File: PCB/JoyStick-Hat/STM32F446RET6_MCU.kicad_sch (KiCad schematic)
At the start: 42 parts, among them J1 20021121-00010C4LF, J16 Conn_01x06, J2 BU2032SM-JJ-GTR, J3 Conn_02x05_Odd_Even, SW1 TL3301NF260QG, U1 STM32F446VETx, X1 ABM3B-8.000MHZ-B2-T, X2 ABS07-32.768KHZ-9-T

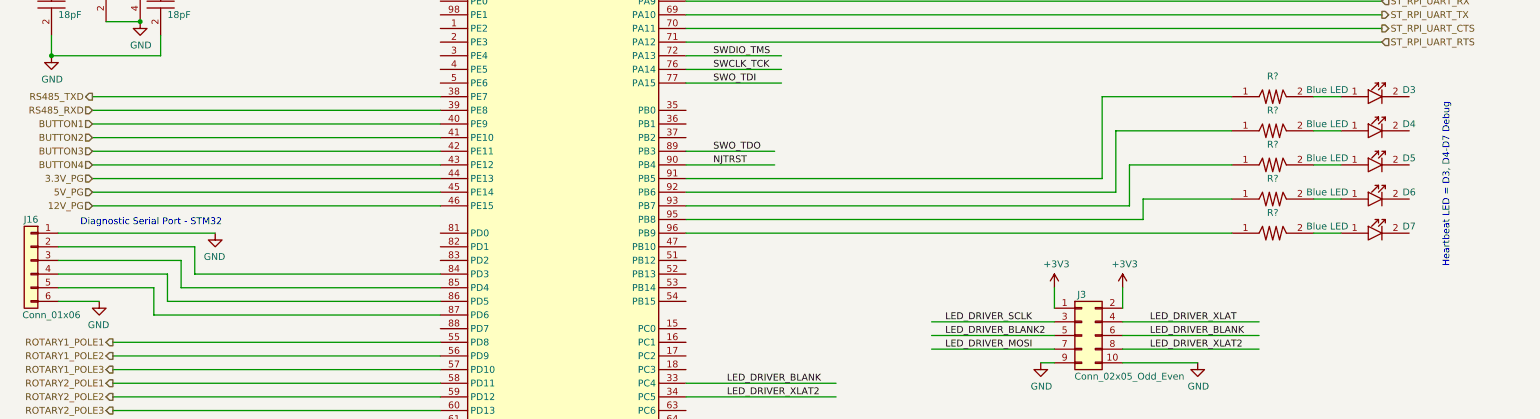
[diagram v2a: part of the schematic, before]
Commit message: Board Routing
Connectors swapped around and board route started
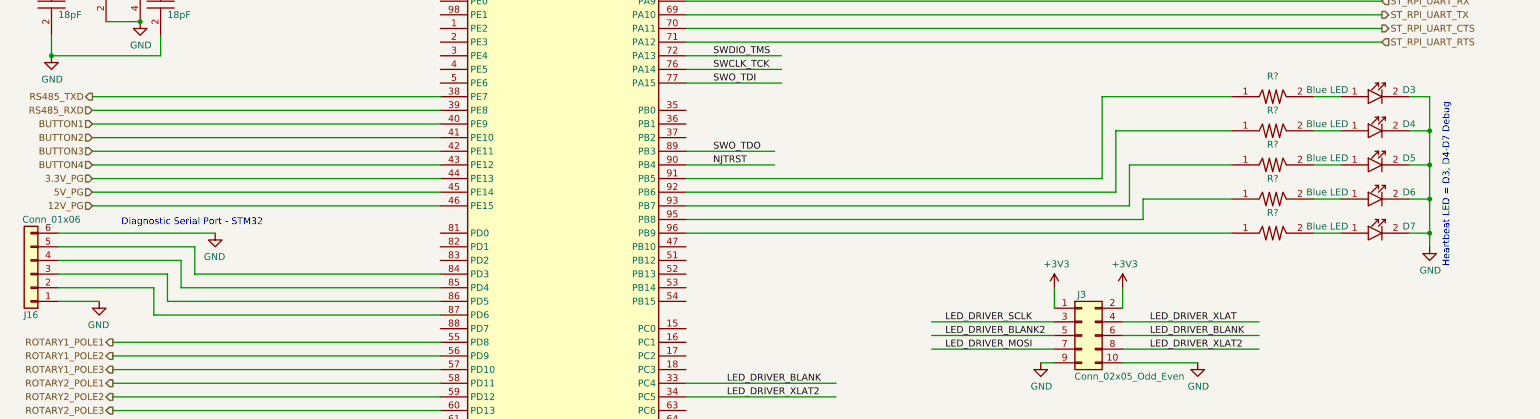
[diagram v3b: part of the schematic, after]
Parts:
- J16: footprint Connector_PinHeader_2.54mm:PinHeader_1x06_P2.54mm_Vertical -> Connector_PinHeader_2.54mm:PinHeader_1x06_P2.54mm_Horizontal
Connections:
- net GND: now also D3.2, D4.2, D5.2, D6.2, D7.2
- net at J16.2 (Pin_2): now also U1.87 (PD6); no longer U1.84 (PD3)
- net at J16.3 (Pin_3): now also U1.86 (PD5); no longer U1.85 (PD4)
- net at J16.4 (Pin_4): now also U1.85 (PD4); no longer U1.86 (PD5)
- net at J16.5 (Pin_5): now also U1.84 (PD3); no longer U1.87 (PD6)
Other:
- moved on the sheet: J16
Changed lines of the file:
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@@
   (junction (at 38.1 39.37) (diameter 0) (color 0 0 0 0)
   )
+  (junction (at 275.59 92.71) (diameter 0) (color 0 0 0 0)
+  )
   (junction (at 19.05 78.74) (diameter 0) (color 0 0 0 0)
   )
@@
   (junction (at 93.98 25.4) (diameter 0) (color 0 0 0 0)
   )
+  (junction (at 275.59 105.41) (diameter 0) (color 0 0 0 0)
+  )
   (junction (at 17.78 166.37) (diameter 0) (color 0 0 0 0)
   )
@@
   (junction (at 63.5 181.61) (diameter 0) (color 0 0 0 0)
   )
+  (junction (at 275.59 111.76) (diameter 0) (color 0 0 0 0)
+  )
   (junction (at 114.3 38.1) (diameter 0) (color 0 0 0 0)
   )
@@
   (junction (at 116.84 38.1) (diameter 0) (color 0 0 0 0)
   )
+  (junction (at 275.59 99.06) (diameter 0) (color 0 0 0 0)
+  )
   (junction (at 135.89 25.4) (diameter 0) (color 0 0 0 0)
   )
@@
     (stroke (width 0) (type default))
   )
-  (wire (pts (xy 20.32 119.38) (xy 40.64 119.38))
-    (stroke (width 0) (type default))
-  )
   (wire (pts (xy 26.67 88.9) (xy 91.44 88.9))
     (stroke (width 0) (type default))
@@
     (stroke (width 0) (type default))
   )
+  (wire (pts (xy 20.32 119.38) (xy 40.64 119.38))
+    (stroke (width 0) (type default))
+  )
   (wire (pts (xy 222.25 109.22) (xy 222.25 105.41))
     (stroke (width 0) (type default))
@@
     (stroke (width 0) (type default))
   )
+  (wire (pts (xy 275.59 105.41) (xy 275.59 111.76))
+    (stroke (width 0) (type default))
+  )
+  (wire (pts (xy 275.59 86.36) (xy 275.59 92.71))
+    (stroke (width 0) (type default))
+  )
+  (wire (pts (xy 20.32 116.84) (xy 43.18 116.84))
+    (stroke (width 0) (type default))
+  )
   (wire (pts (xy 19.05 33.02) (xy 19.05 39.37))
     (stroke (width 0) (type default))
@@
     (stroke (width 0) (type default))
   )
+  (wire (pts (xy 271.78 105.41) (xy 275.59 105.41))
+    (stroke (width 0) (type default))
+  )
   (wire (pts (xy 182.88 29.21) (xy 190.5 29.21))
     (stroke (width 0) (type default))
@@
     (stroke (width 0) (type default))
   )
+  (wire (pts (xy 271.78 92.71) (xy 275.59 92.71))
+    (stroke (width 0) (type default))
+  )
   (wire (pts (xy 175.26 29.21) (xy 182.88 29.21))
     (stroke (width 0) (type default))
@@
     (stroke (width 0) (type default))
   )
-  (wire (pts (xy 20.32 114.3) (xy 45.72 114.3))
-    (stroke (width 0) (type default))
-  )
   (wire (pts (xy 121.92 17.78) (xy 121.92 38.1))
     (stroke (width 0) (type default))
@@
     (stroke (width 0) (type default))
   )
+  (wire (pts (xy 275.59 111.76) (xy 275.59 114.3))
+    (stroke (width 0) (type default))
+  )
   (wire (pts (xy 116.84 177.8) (xy 114.3 177.8))
     (stroke (width 0) (type default))
@@
     (stroke (width 0) (type default))
   )
+  (wire (pts (xy 271.78 86.36) (xy 275.59 86.36))
+    (stroke (width 0) (type default))
+  )
   (wire (pts (xy 218.44 130.81) (xy 243.84 130.81))
     (stroke (width 0) (type default))
@@
     (stroke (width 0) (type default))
   )
+  (wire (pts (xy 20.32 114.3) (xy 45.72 114.3))
+    (stroke (width 0) (type default))
+  )
   (wire (pts (xy 254 111.76) (xy 259.08 111.76))
     (stroke (width 0) (type default))
@@
     (stroke (width 0) (type default))
   )
+  (wire (pts (xy 20.32 121.92) (xy 38.1 121.92))
+    (stroke (width 0) (type default))
+  )
   (wire (pts (xy 30.48 170.18) (xy 63.5 170.18))
     (stroke (width 0) (type default))
@@
     (stroke (width 0) (type default))
   )
+  (wire (pts (xy 275.59 92.71) (xy 275.59 99.06))
+    (stroke (width 0) (type default))
+  )
   (wire (pts (xy 114.3 177.8) (xy 114.3 181.61))
     (stroke (width 0) (type default))
@@
     (stroke (width 0) (type default))
   )
+  (wire (pts (xy 275.59 99.06) (xy 275.59 105.41))
+    (stroke (width 0) (type default))
+  )
   (wire (pts (xy 137.16 152.4) (xy 204.47 152.4))
     (stroke (width 0) (type default))
   )
-  (wire (pts (xy 88.9 180.34) (xy 88.9 191.77))
+  (wire (pts (xy 271.78 111.76) (xy 275.59 111.76))
     (stroke (width 0) (type default))
   )
-  (wire (pts (xy 38.1 121.92) (xy 20.32 121.92))
+  (wire (pts (xy 88.9 180.34) (xy 88.9 191.77))
     (stroke (width 0) (type default))
   )
-  (wire (pts (xy 20.32 111.76) (xy 49.53 111.76))
+  (wire (pts (xy 271.78 99.06) (xy 275.59 99.06))
     (stroke (width 0) (type default))
   )
@@
     (stroke (width 0) (type default))
   )
-  (wire (pts (xy 43.18 116.84) (xy 20.32 116.84))
+  (wire (pts (xy 111.76 38.1) (xy 114.3 38.1))
     (stroke (width 0) (type default))
   )
-  (wire (pts (xy 111.76 38.1) (xy 114.3 38.1))
+  (wire (pts (xy 20.32 111.76) (xy 49.53 111.76))
     (stroke (width 0) (type default))
   )
@@
     (effects (font (size 4 4) (thickness 0.8) bold) (justify left bottom))
   )
-  (text "Diagnostic Serial Port - STM32" (at 50.8 110.49 0)
+  (text "Diagnostic Serial Port - STM32" (at 58.42 110.49 0)
     (effects (font (size 1.27 1.27)) (justify right bottom))
   )
@@
     )
   )
-  (symbol (lib_id "Connector_Generic:Conn_01x06") (at 15.24 116.84 0) (mirror y) (unit 1)
+  (symbol (lib_id "Connector_Generic:Conn_01x06") (at 15.24 119.38 180) (unit 1)
     (in_bom yes) (on_board yes) (dnp no)
-    (property "Reference" "J16" (at 15.24 109.22 0)
+    (property "Reference" "J16" (at 15.24 127 0)
       (effects (font (size 1.27 1.27)))
     )
-    (property "Value" "Conn_01x06" (at 19.05 127 0)
+    (property "Value" "Conn_01x06" (at 19.05 109.22 0)
       (effects (font (size 1.27 1.27)))
     )
-    (property "Footprint" "Connector_PinHeader_2.54mm:PinHeader_1x06_P2.54mm_Vertical" (at 15.24 116.84 0)
+    (property "Footprint" "Connector_PinHeader_2.54mm:PinHeader_1x06_P2.54mm_Horizontal" (at 15.24 119.38 0)
       (effects (font (size 1.27 1.27)) hide)
     )
-    (property "Datasheet" "~" (at 15.24 116.84 0)
+    (property "Datasheet" "~" (at 15.24 119.38 0)
       (effects (font (size 1.27 1.27)) hide)
     )
@@
         )
       )
+    )
+  )
+  (symbol (lib_id "power:GND") (at 275.59 114.3 0) (unit 1)
+    (in_bom yes) (on_board yes) (dnp no)
+    (property "Reference" "#PWR022" (at 275.59 120.65 0)
+      (effects (font (size 1.27 1.27)) hide)
+    )
+    (property "Value" "GND" (at 275.717 118.6942 0)
+      (effects (font (size 1.27 1.27)))
+    )
+    (property "Footprint" "" (at 275.59 114.3 0)
+      (effects (font (size 1.27 1.27)) hide)
+    )
+    (property "Datasheet" "" (at 275.59 114.3 0)
+      (effects (font (size 1.27 1.27)) hide)
+    )
+    (pin "1")
+    (instances
+      (project "JoyStick-Hat"
+        (path "/cf0c81b5-5bdf-47c3-83c0-f6980f515e65/edccb318-6986-4250-98d3-482c4b5ba7f8"
+          (reference "#PWR022") (unit 1)
+        )
+      )
+      (project "agricoltura-vine"
+        (path "/d9101753-24ed-41f7-9f75-798d6e08c38a/00000000-0000-0000-0000-00005ee8264d"
+          (reference "#PWR?") (unit 1)
+        )
+      )

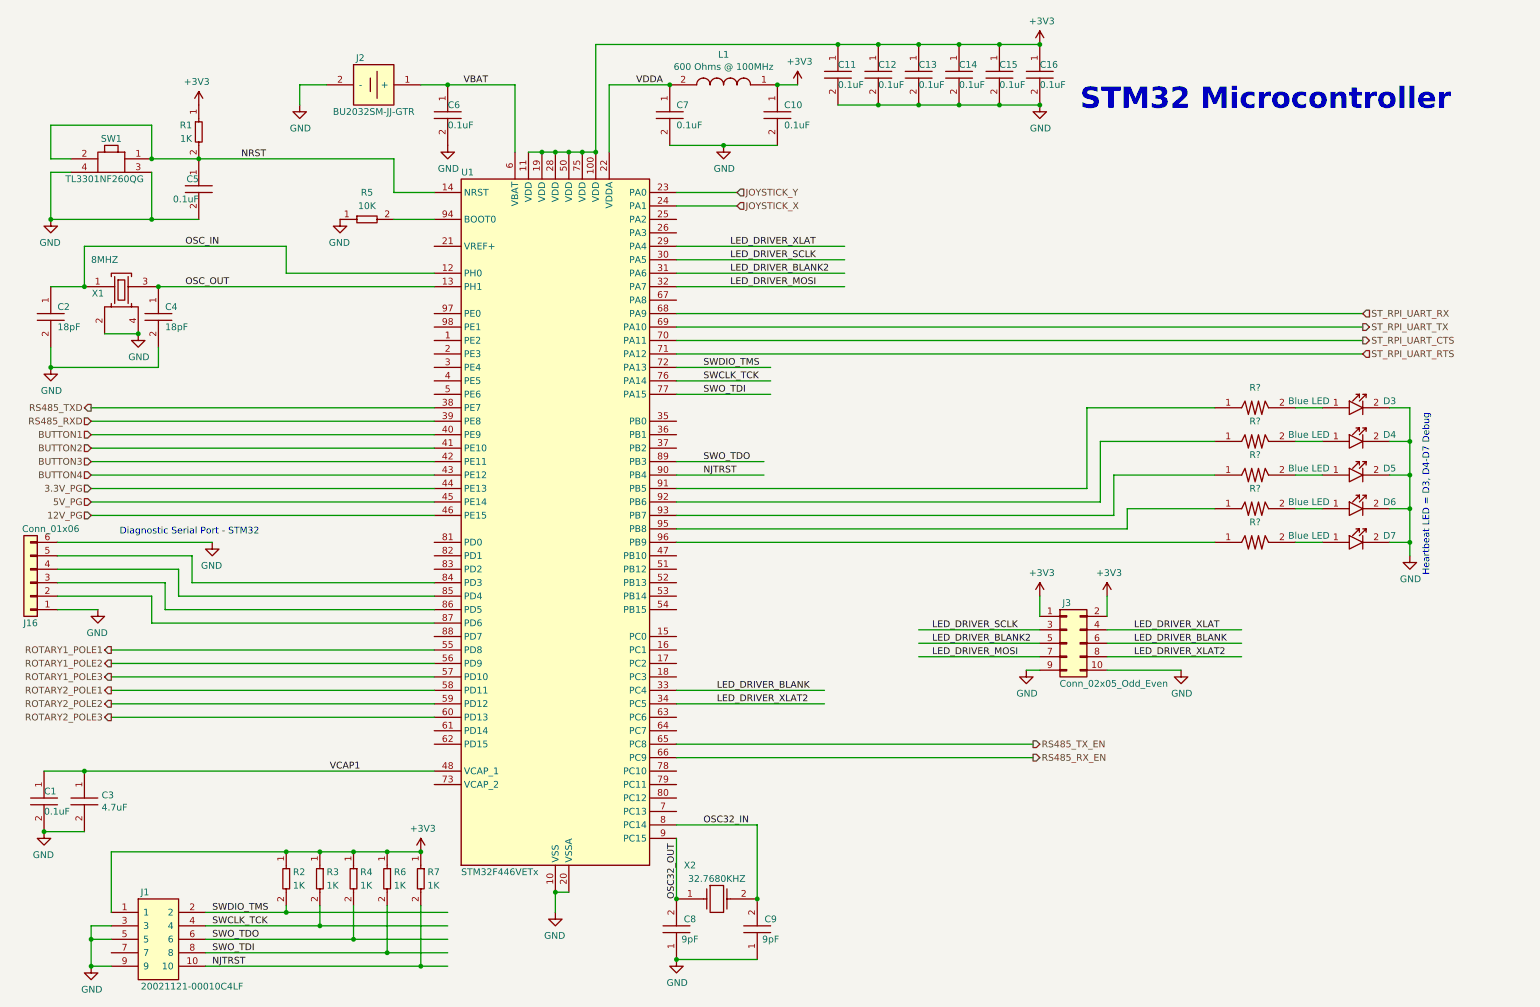
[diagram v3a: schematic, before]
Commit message: Board Progress
Board route nearly complete, internal power plane topologys witched up to run 5Vs as plane. Reset buttom moved. Next: add more LEDs and breakout more STM32 pins for development purposes.
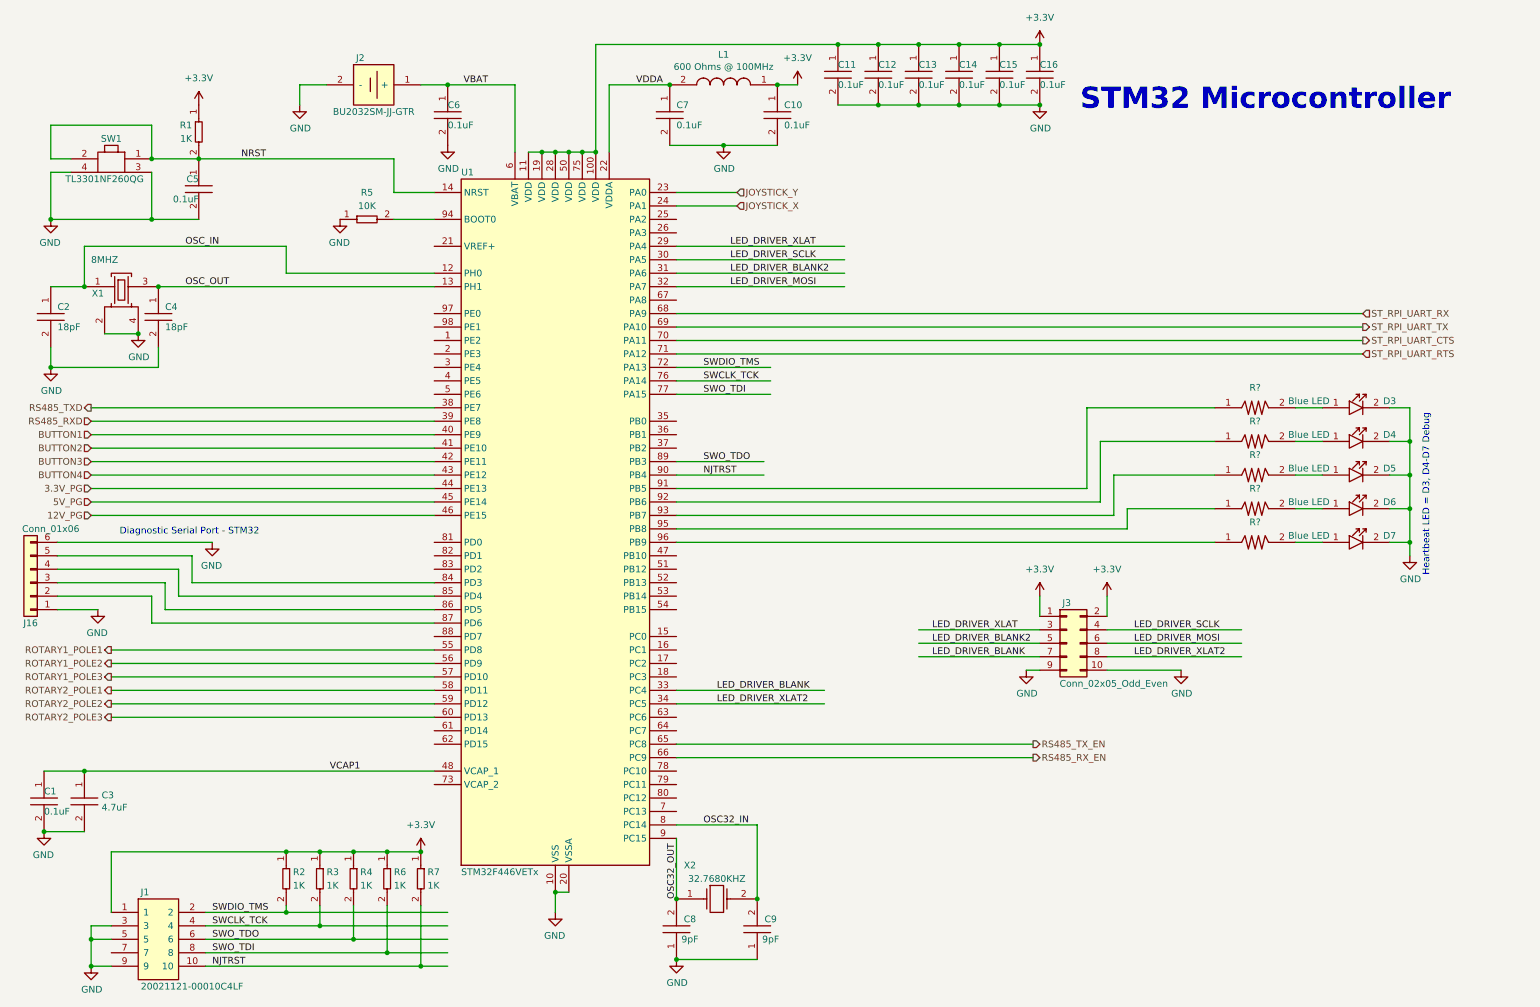
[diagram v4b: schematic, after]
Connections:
- net LED_DRIVER_BLANK: now also J3.7 (Pin_7); no longer J3.6 (Pin_6)
- net LED_DRIVER_MOSI: now also J3.6 (Pin_6); no longer J3.7 (Pin_7)
- net LED_DRIVER_SCLK: now also J3.4 (Pin_4); no longer J3.3 (Pin_3)
- net LED_DRIVER_XLAT: now also J3.3 (Pin_3); no longer J3.4 (Pin_4)
- net +3V3 renamed +3.3V

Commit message: PCB First Pass Complete
First complete pass at PCB finished. Added more debug LEDs for both STM32 and RPi, 8 totaly so binary data can be outputted as a byte etc, that way we can have debug codes. Added heartbeat LED to STM32. Rearranged connectors and pinning of certain connectors to make routing smooth and traces short.
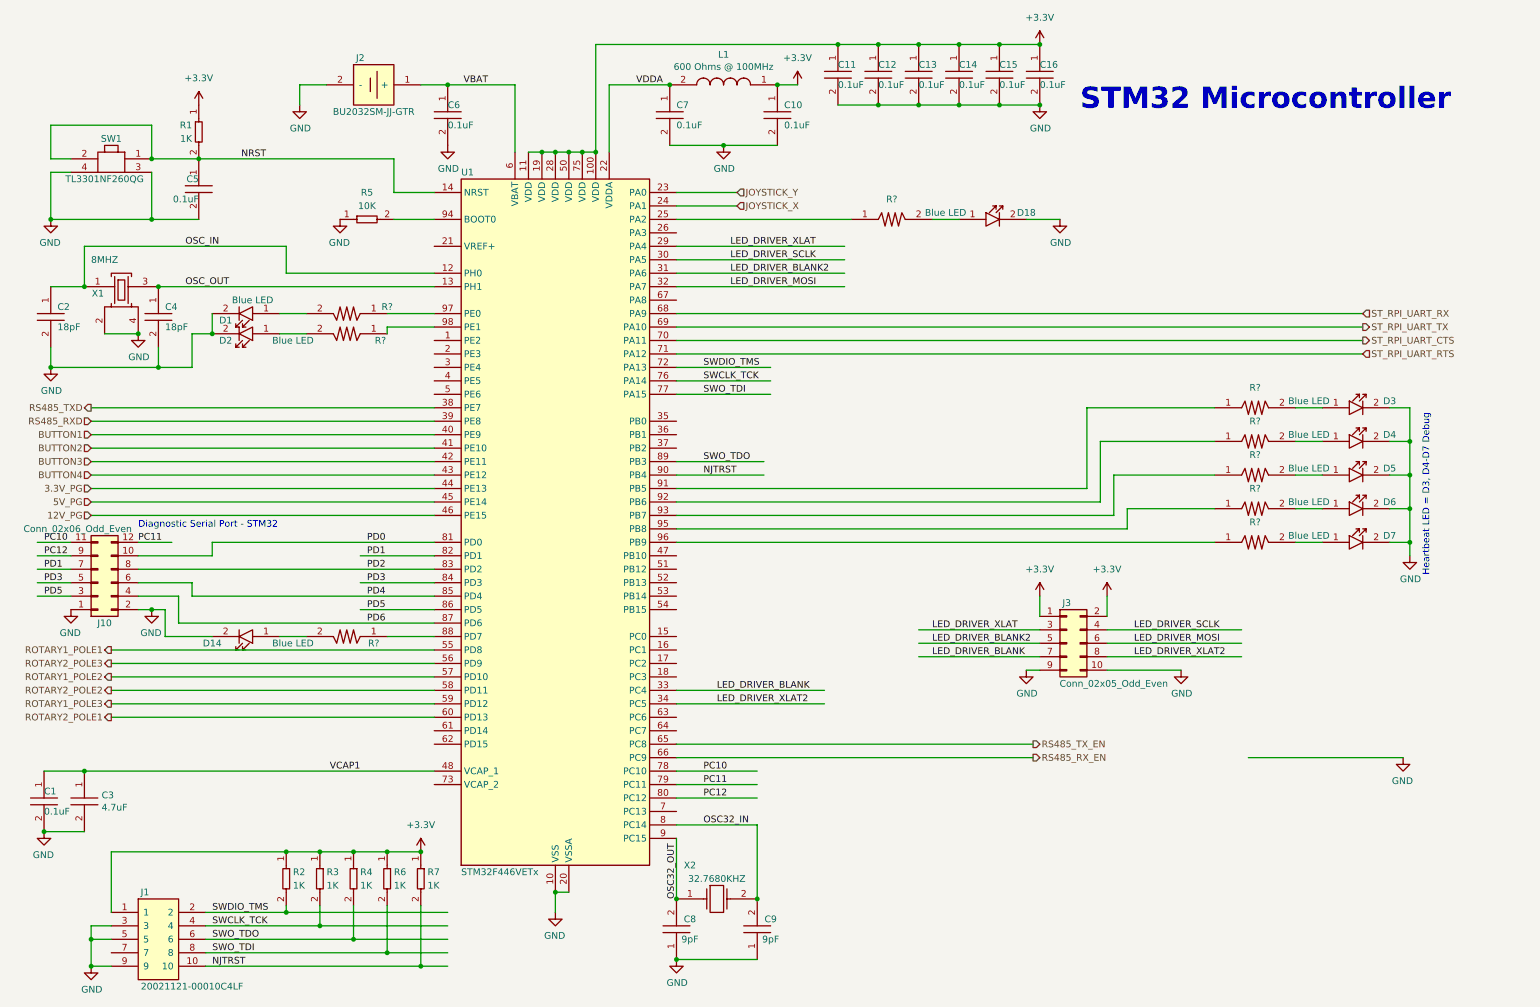
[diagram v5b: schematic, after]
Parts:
- removed J16: Conn_01x06, Connector_PinHeader_2.54mm:PinHeader_1x06_P2.54mm_Horizontal, symbol Connector_Generic:Conn_01x06
- added D1, D14, D18, D2: LTST-C194TBKT, AVR-KiCAD-Lib-Diodes:LED0603, symbol AVR-KiCAD-Lib-Diodes:LTST-C194TBKT
- added J10: Conn_02x06_Odd_Even, Connector_PinHeader_2.54mm:PinHeader_2x06_P2.54mm_Horizontal, symbol Connector_Generic:Conn_02x06_Odd_Even
- added R? (x4): RC0603FR-07470RL, AVR-KiCAD-Lib-Resistors:R0603, symbol AVR-KiCAD-Lib-Resistors:RC0603FR-07470RL
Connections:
- net GND: now also D1.2, D14.2, D18.2, D2.2, J10.1 (Pin_1), J10.2 (Pin_2)
- net ROTARY1_POLE2: now also U1.57 (PD10); no longer U1.56 (PD9)
- net ROTARY1_POLE3: now also U1.59 (PD12); no longer U1.57 (PD10)
- net ROTARY2_POLE1: now also U1.60 (PD13); no longer U1.58 (PD11)
- net ROTARY2_POLE2: now also U1.58 (PD11); no longer U1.59 (PD12)
- net ROTARY2_POLE3: now also U1.56 (PD9); no longer U1.60 (PD13)
- net PD6: now reaches U1.87 (PD6)
- net PD6: now also J10.4 (Pin_4)
- net PD5: now reaches U1.86 (PD5)
- net PD5: now also J10.3 (Pin_3)
- net PD4: now reaches U1.85 (PD4)
- net PD4: now also J10.6 (Pin_6)
- net PD3: now reaches U1.84 (PD3)
- net PD3: now also J10.5 (Pin_5)
- net at U1.25 (PA2): now also R?.1
- net PC10: now reaches U1.78 (PC10)
- net PC10: now also J10.11 (Pin_11)
- net PC11: now reaches U1.79 (PC11)
- net PC11: now also J10.12 (Pin_12)
- net PC12: now reaches U1.80 (PC12)
- net PC12: now also J10.9 (Pin_9)
- net PD0: now reaches U1.81 (PD0)
- net PD0: now also J10.10 (Pin_10)
- net PD1: now reaches U1.82 (PD1)
- net PD1: now also J10.7 (Pin_7)
- net PD2: now reaches U1.83 (PD2)
- net PD2: now also J10.8 (Pin_8)
- net at U1.88 (PD7): now also R?.1
- net at U1.97 (PE0): now also R?.1
- net at U1.98 (PE1): now also R?.1
- new net: D2.1, R?.2
- new net: D14.1, R?.2
- new net: D18.1, R?.2
- new net: D1.1, R?.2

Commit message: James Fixes and 3D models
Added all the changes that James suggested to the design and then added 3D models to the board for mechanical design purposes. Generated 3D renders of the board and added them to new directory called img.
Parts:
- gave numbers to parts that had none: 9
